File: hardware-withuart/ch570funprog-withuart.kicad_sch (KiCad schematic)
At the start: 25 parts, among them J1 USB_C_Receptacle_USB2.0, J2 PGM, Q1 PMOS-SI2301CDS-T1-GE3, U1 USBPROT, U2 AMS1117-3.3, U3 CH570Q, Y1 32M

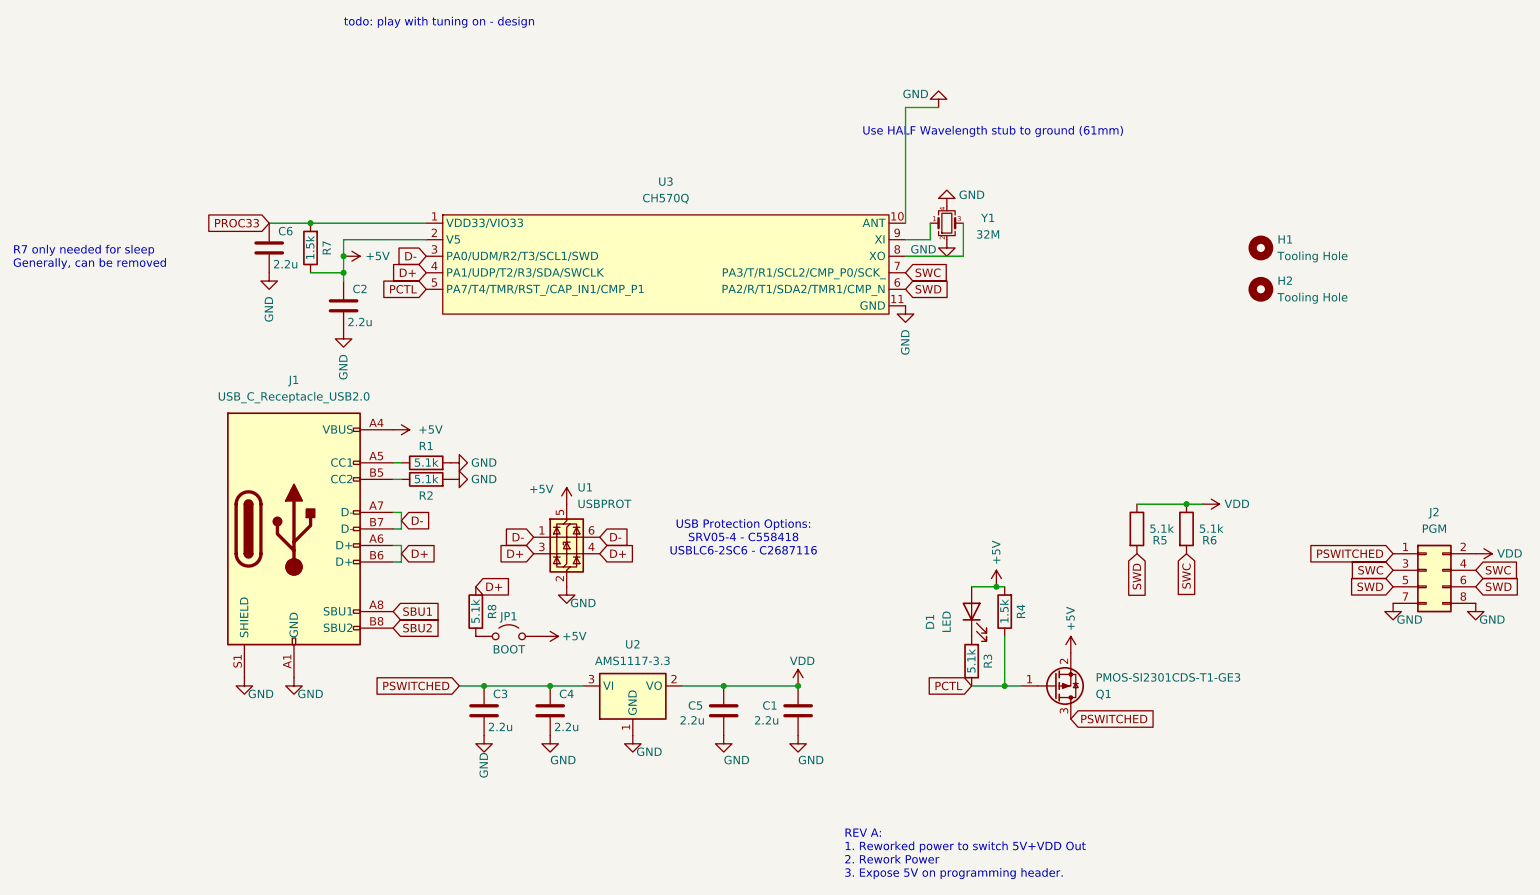
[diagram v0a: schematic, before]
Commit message: Add delay for boot Add ch570funprog with uart
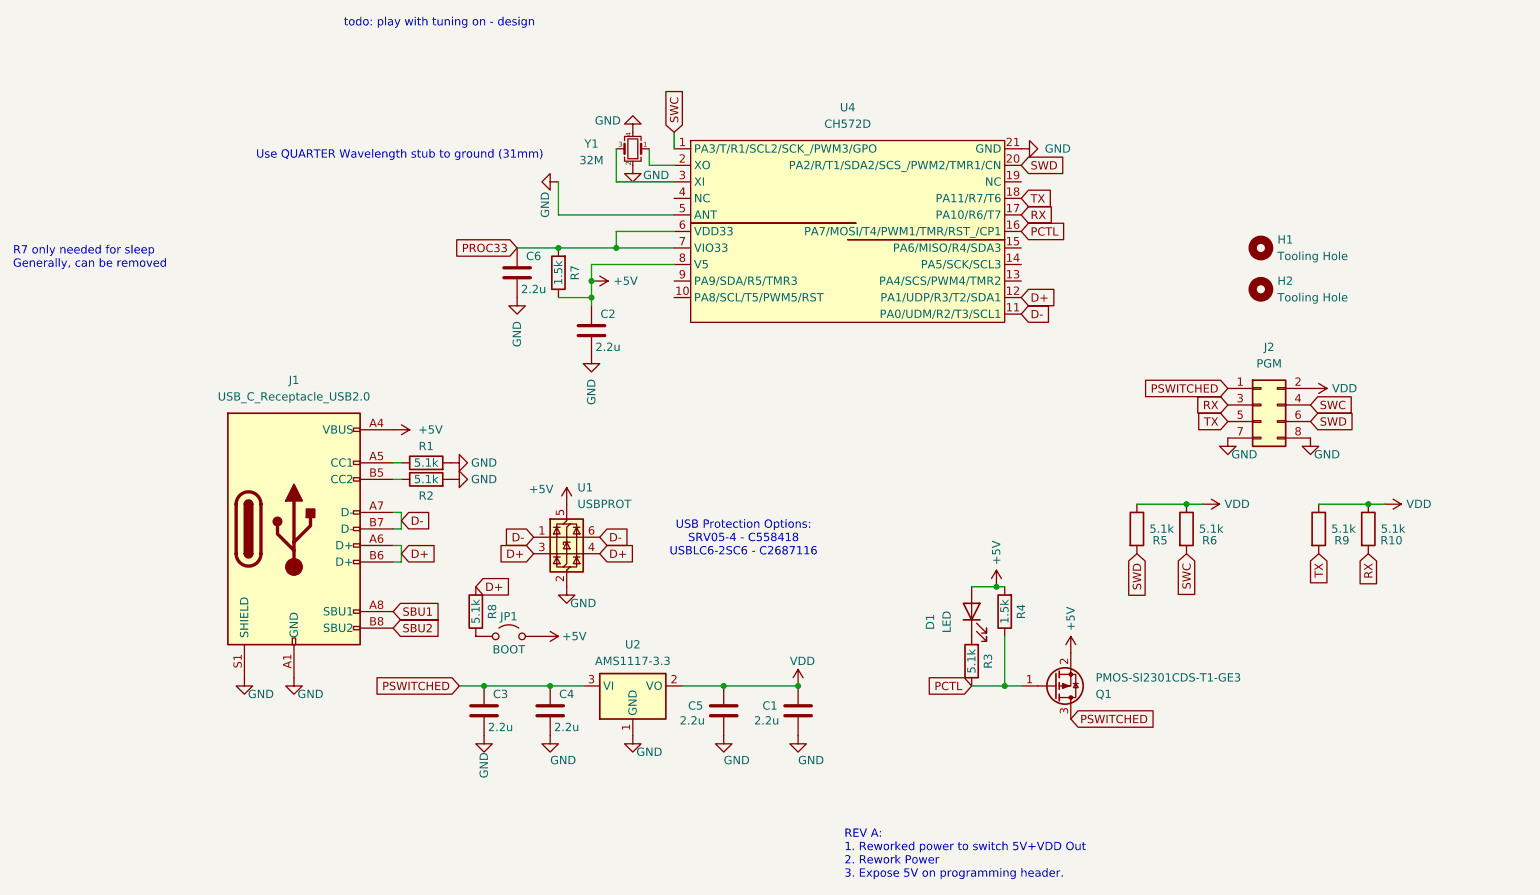
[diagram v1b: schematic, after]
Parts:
- removed U3: CH570Q, Package_DFN_QFN:DFN-10-1EP_3x3mm_P0.5mm_EP1.7x2.5mm, symbol cnhardware:CH570Q
- added R10, R9: 5.1k, Resistor_SMD:R_0402_1005Metric, symbol Device:R
- added U4: CH572D, Package_DFN_QFN:QFN-20-1EP_3x3mm_P0.4mm_EP1.65x1.65mm, symbol cnhardware:CH570D
- JP1: footprint Jumper:SolderJumper-2_P1.3mm_Open_RoundedPad1.0x1.5mm -> Jumper:SolderJumper-2_P1.3mm_Open_TrianglePad1.0x1.5mm
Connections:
- net +5V: now also U4.8 (V5)
- net D+: now also U4.12 (PA1/UDP/R3/T2/SDA1)
- net D-: now also U4.11 (PA0/UDM/R2/T3/SCL1)
- net GND: now also U4.21 (GND), U4.5 (ANT)
- net PCTL: now also U4.16 (PA7/MOSI/T4/PWM1/TMR/RST_/CP1)
- net PROC33: now also U4.6 (VDD33), U4.7 (VIO33)
- net SWC: now also U4.1 (PA3/T/R1/SCL2/SCK_/PWM3/GPO); no longer J2.3 (Pin_3)
- net SWD: now also U4.20 (PA2/R/T1/SDA2/SCS_/PWM2/TMR1/CN); no longer J2.5 (Pin_5)
- net VDD: now also R10.1, R9.1
- net at Y1.1: now also U4.2 (XO)
- net at Y1.3: now also U4.3 (XI)
- new net RX: J2.3 (Pin_3), R10.2, U4.17 (PA10/R6/T7)
- new net TX: J2.5 (Pin_5), R9.2, U4.18 (PA11/R7/T6)
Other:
- note added: "Use QUARTER Wavelength stub to ground (31mm)"
- note removed: "Use HALF Wavelength stub to ground (61mm)"
- moved on the sheet: C2, C6, J2, R7
